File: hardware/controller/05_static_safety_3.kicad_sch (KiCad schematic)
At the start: 12 parts

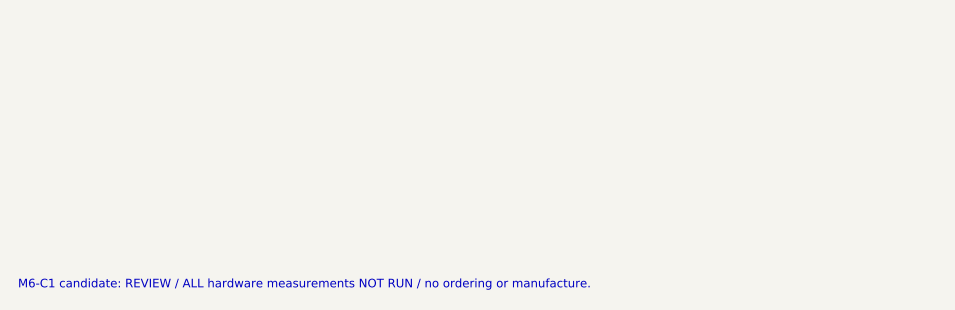
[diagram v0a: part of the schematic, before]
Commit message: M6-C1R1: protect pack identity input and review USB ESD topology
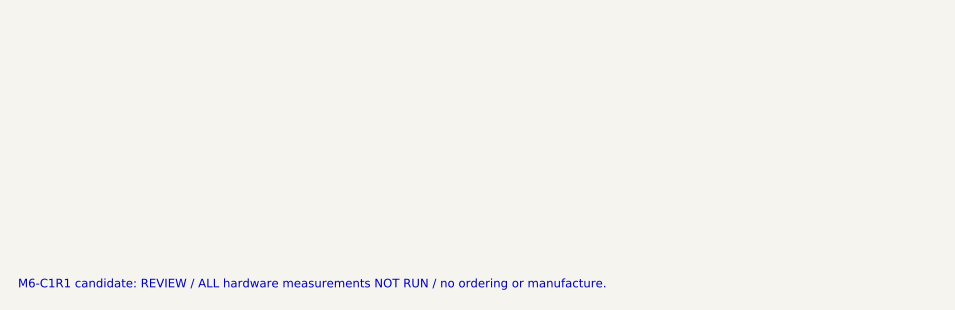
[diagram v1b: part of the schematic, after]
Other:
- note added: "M6-C1R1 candidate: REVIEW / ALL hardware measurements NOT RUN / no ordering or manufacture."
- note removed: "M6-C1 candidate: REVIEW / ALL hardware measurements NOT RUN / no ordering or manufacture."
